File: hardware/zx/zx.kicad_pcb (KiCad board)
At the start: 2 copper layers, 71.6 x 59.9 mm, 47 parts, among them J1 ZX Keyboard, J10 Conn_01x01, J11 Conn_01x01, J12 Conn_01x01, J13 Conn_01x01, J14 Conn_01x01, J15 Conn_01x01, J16 Conn_01x01, J17 Conn_01x01, J18 Conn_01x01, J19 Conn_01x01, J2 GOTEK, J20 Conn_01x01, J21 Conn_01x01, J22 Conn_01x01, J23 Conn_01x01, J24 Conn_01x01, J25 Conn_01x01, J26 Conn_01x01, J3 UART, J4 USB_A, J5 USB_A, J6 Keyboard, J7 Mouse, J8 Kempston Mouse, J9 Z80, SW1 RESET, SW2 BOOT0, SW3 BOOT1, U1 CH559L, U2 CH446Q, Y1 12MHz

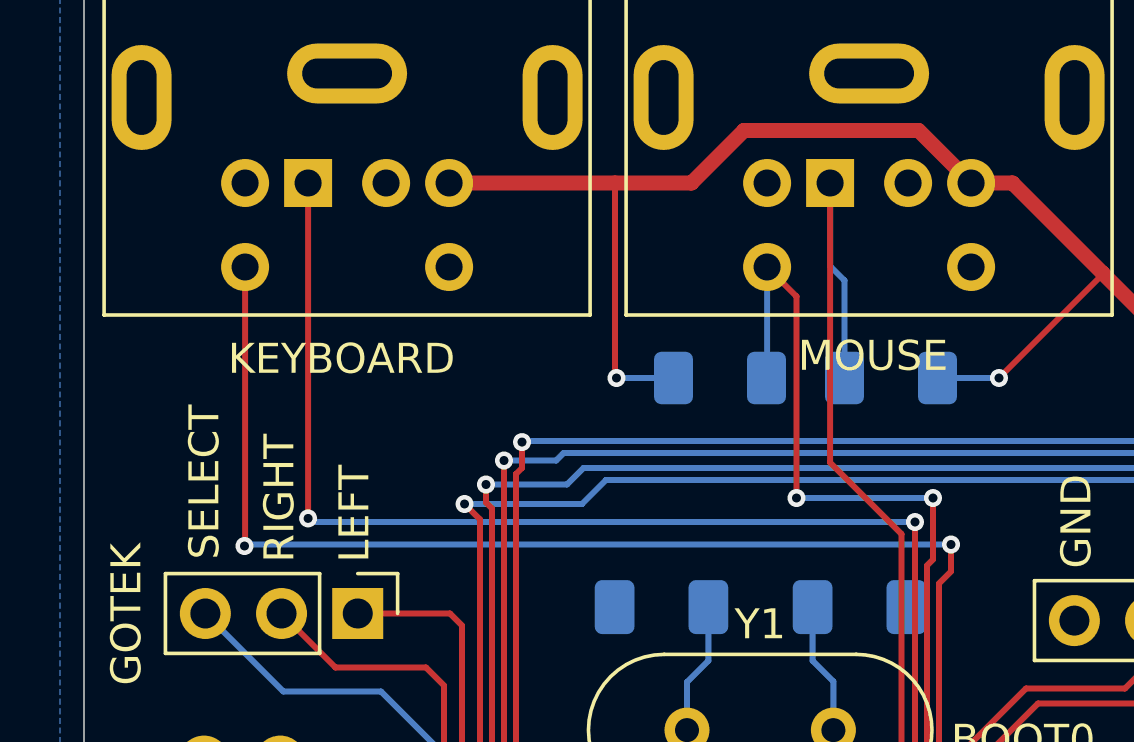
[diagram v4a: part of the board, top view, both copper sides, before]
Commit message: Add PS/2 keyboard/mouse debug pins.
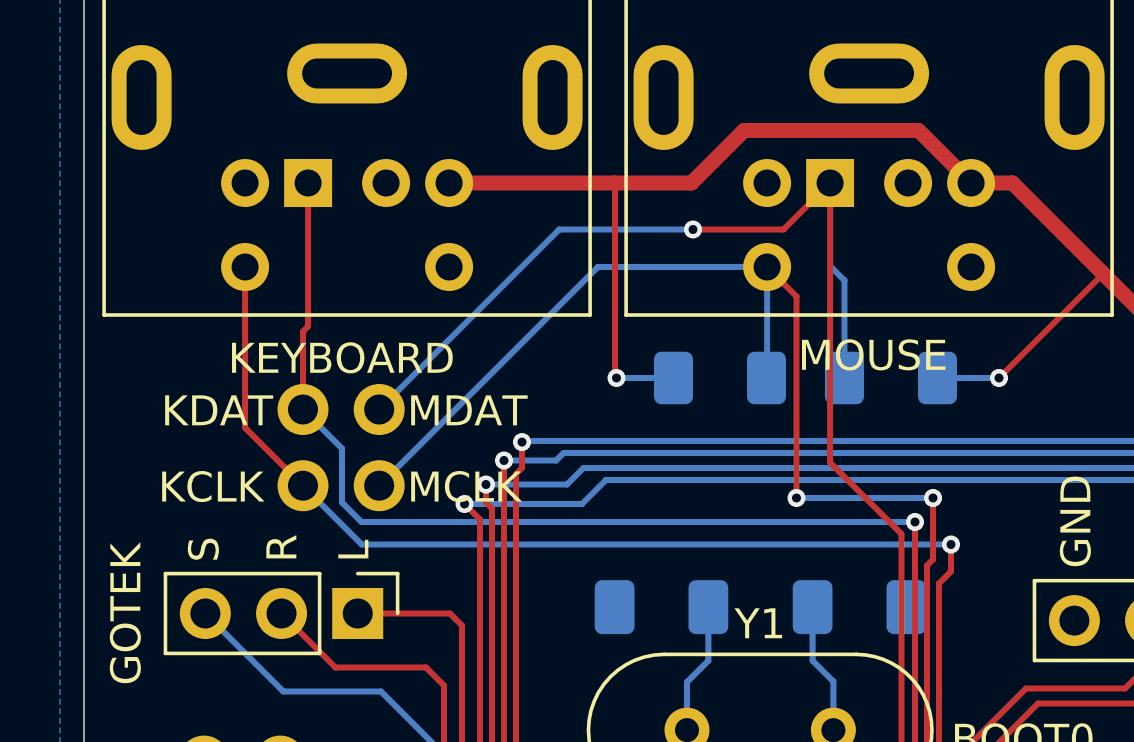
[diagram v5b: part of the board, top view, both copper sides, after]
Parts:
- added J27: Conn_01x01, THT_Pin:THT_Pin_Vertical, F.Cu at (107.3, 116.3)
- added J28: Conn_01x01, THT_Pin:THT_Pin_Vertical, F.Cu at (107.3, 118.8)
- added J29: Conn_01x01, THT_Pin:THT_Pin_Vertical, F.Cu at (109.8, 116.3)
- added J30: Conn_01x01, THT_Pin:THT_Pin_Vertical, F.Cu at (109.8, 118.8)
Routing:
- net /M_DAT: track 35.5 -> 53.6 mm, vias 0 -> 1
- net /M_CLK: track 35.2 -> 51.1 mm
- net /KEY_CLK: track 50.9 -> 48.5 mm, vias 2 -> 1
- net /KEY_DAT: track 48.7 -> 47.8 mm, vias 2 -> 1
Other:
- board text added: "KCLK"
- board text added: "KDAT"
- board text added: "L"
- board text added: "MCLK"
- board text added: "MDAT"
- board text added: "R"
- board text added: "S"
- board text removed: "LEFT"
- board text removed: "RIGHT"
- board text removed: "SELECT"
